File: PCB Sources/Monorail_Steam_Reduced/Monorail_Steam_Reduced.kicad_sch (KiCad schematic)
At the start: 185 parts, among them J1 USB_C_Receptacle_USB2.0, J10 Conn_01x09, J2 USB_C_Receptacle_USB2.0, J4 Conn_01x04_Male, J5 Conn_01x04_Female, J6 Conn_01x03_Male, J7 Conn_01x09, J8 Conn_01x05, J9 Conn_01x05, SW1 RotaryEncoder_Switch, SW2 RotaryEncoder_Switch, SW3 RotaryEncoder_Switch, U1 SRV05-4, U2 XC6206PxxxMR, U3 RP2040TR7, U4 W25Q128JVS, Y1 Crystal_GND24_Small

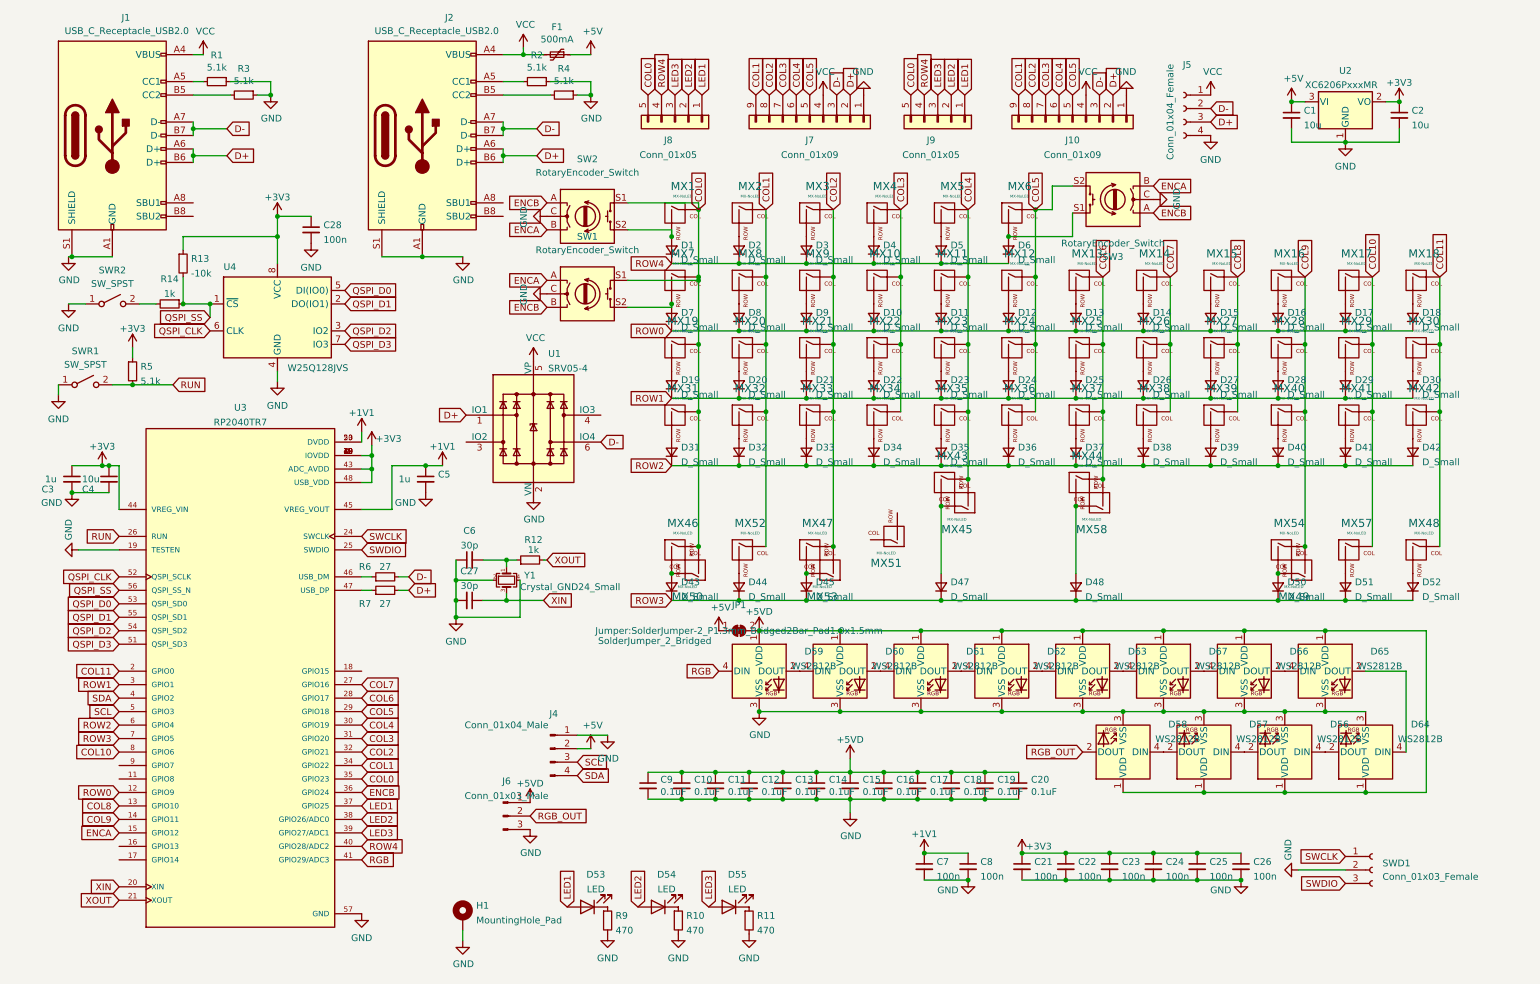
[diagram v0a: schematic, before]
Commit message: updated pcb: deleted num-row, new bottom row
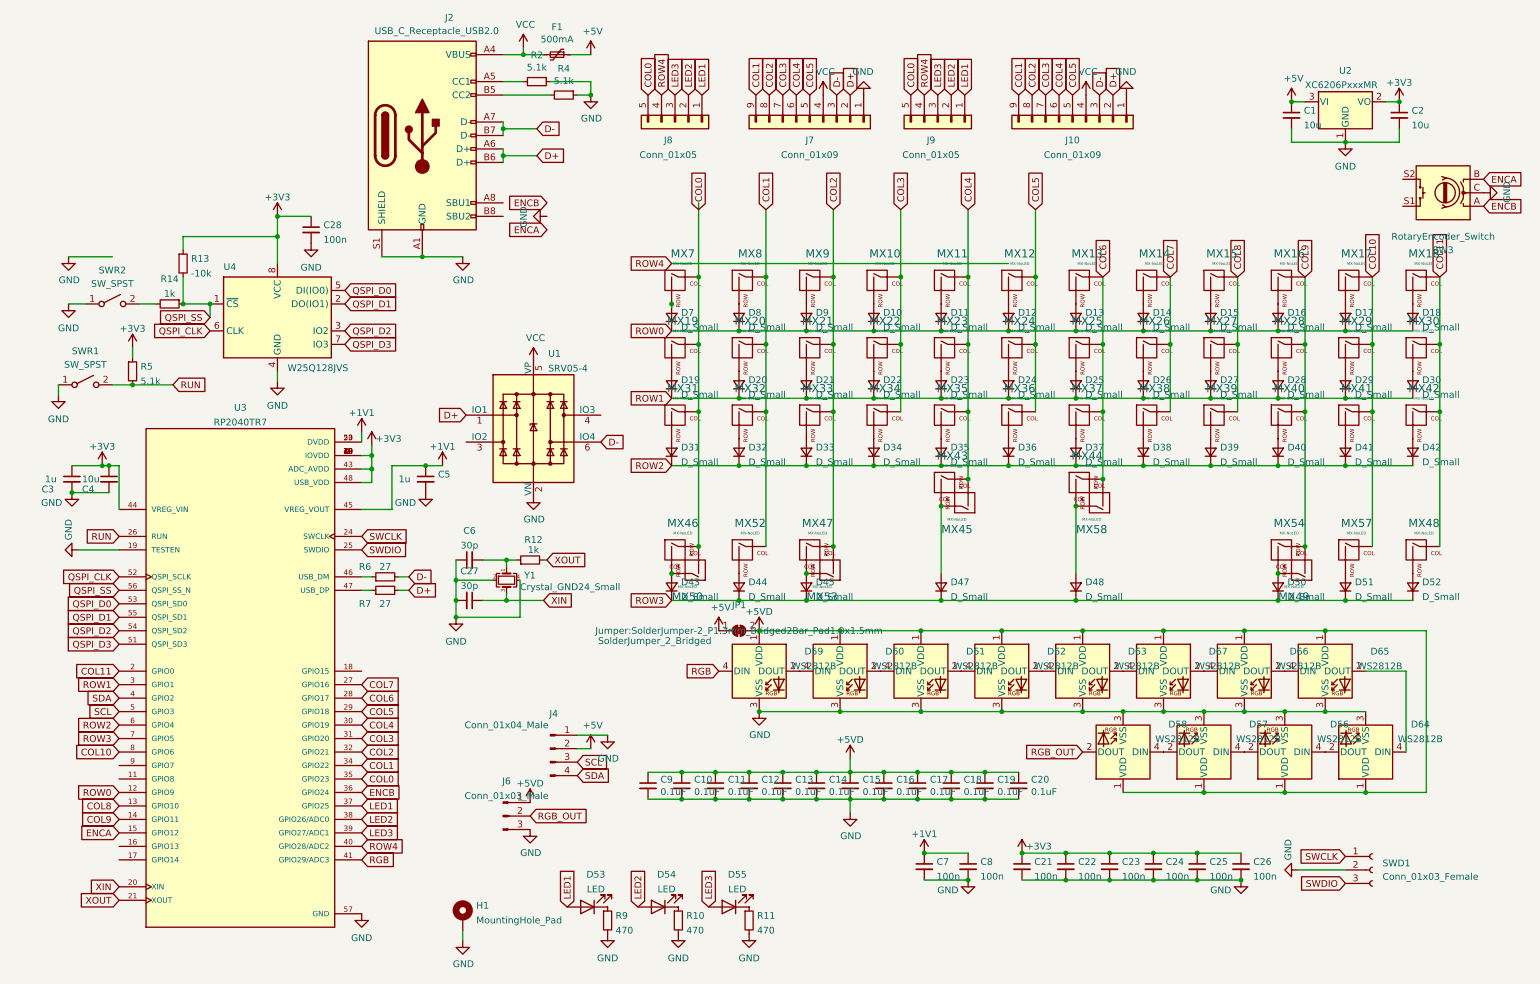
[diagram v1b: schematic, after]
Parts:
- removed D1, D2, D3, D4, D5, D6: D_Small, Diode_SMD:D_SOD-123, symbol Device:D_Small
- removed J1: USB_C_Receptacle_USB2.0, Keebio-Parts:USB_C_Receptacle_HRO_TYPE-C-31-M-12, symbol Connector:USB_C_Receptacle_USB2.0
- removed J5: Conn_01x04_Female, Connector_JST:JST_SH_SM04B-SRSS-TB_1x04-1MP_P1.00mm_Horizontal, symbol Connector:Conn_01x04_Female
- removed MX1, MX2, MX3, MX4, MX5, MX6: MX-NoLED, MX_Only:MXOnly-1U-Hotswap, symbol MX_Alps_Hybrid:MX-NoLED
- removed MX51: MX-NoLED, MX_Only:MXOnly-1.25U-Hotswap, symbol MX_Alps_Hybrid:MX-NoLED
- removed R1, R3: 5.1k, Resistor_SMD:R_0603_1608Metric, symbol Device:R_Small
- removed SW1, SW2: RotaryEncoder_Switch, kiserdesigns:RotaryEncoder_Alps_EC11E-Switch_Vertical_H20mm, symbol Device:RotaryEncoder_Switch
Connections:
- net COL5: no longer SW3.S2
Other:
- moved on the sheet: SW3

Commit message: removed unecessary files, cleaned pcb
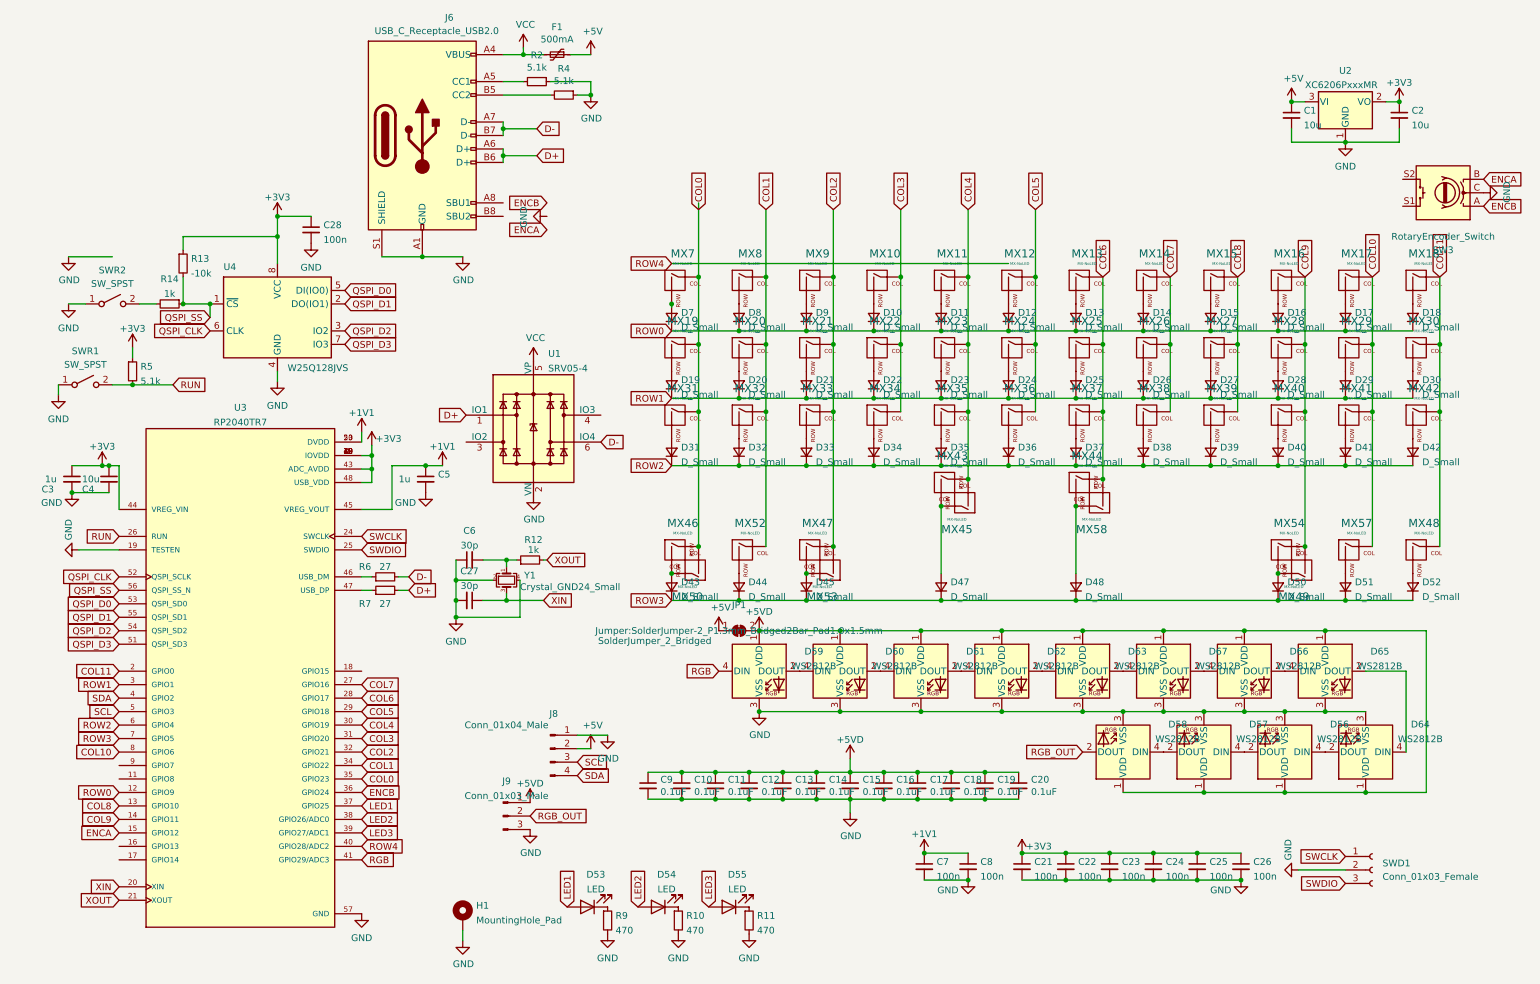
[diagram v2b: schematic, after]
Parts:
- removed J10, J7: Conn_01x09, Connector_PinHeader_2.54mm:PinHeader_1x09_P2.54mm_Vertical, symbol Connector_Generic:Conn_01x09
- removed J8, J9: Conn_01x05, Connector_PinHeader_2.54mm:PinHeader_1x05_P2.54mm_Vertical, symbol Connector_Generic:Conn_01x05
- renumbered J2 to J6, J4 to J8, J6 to J9

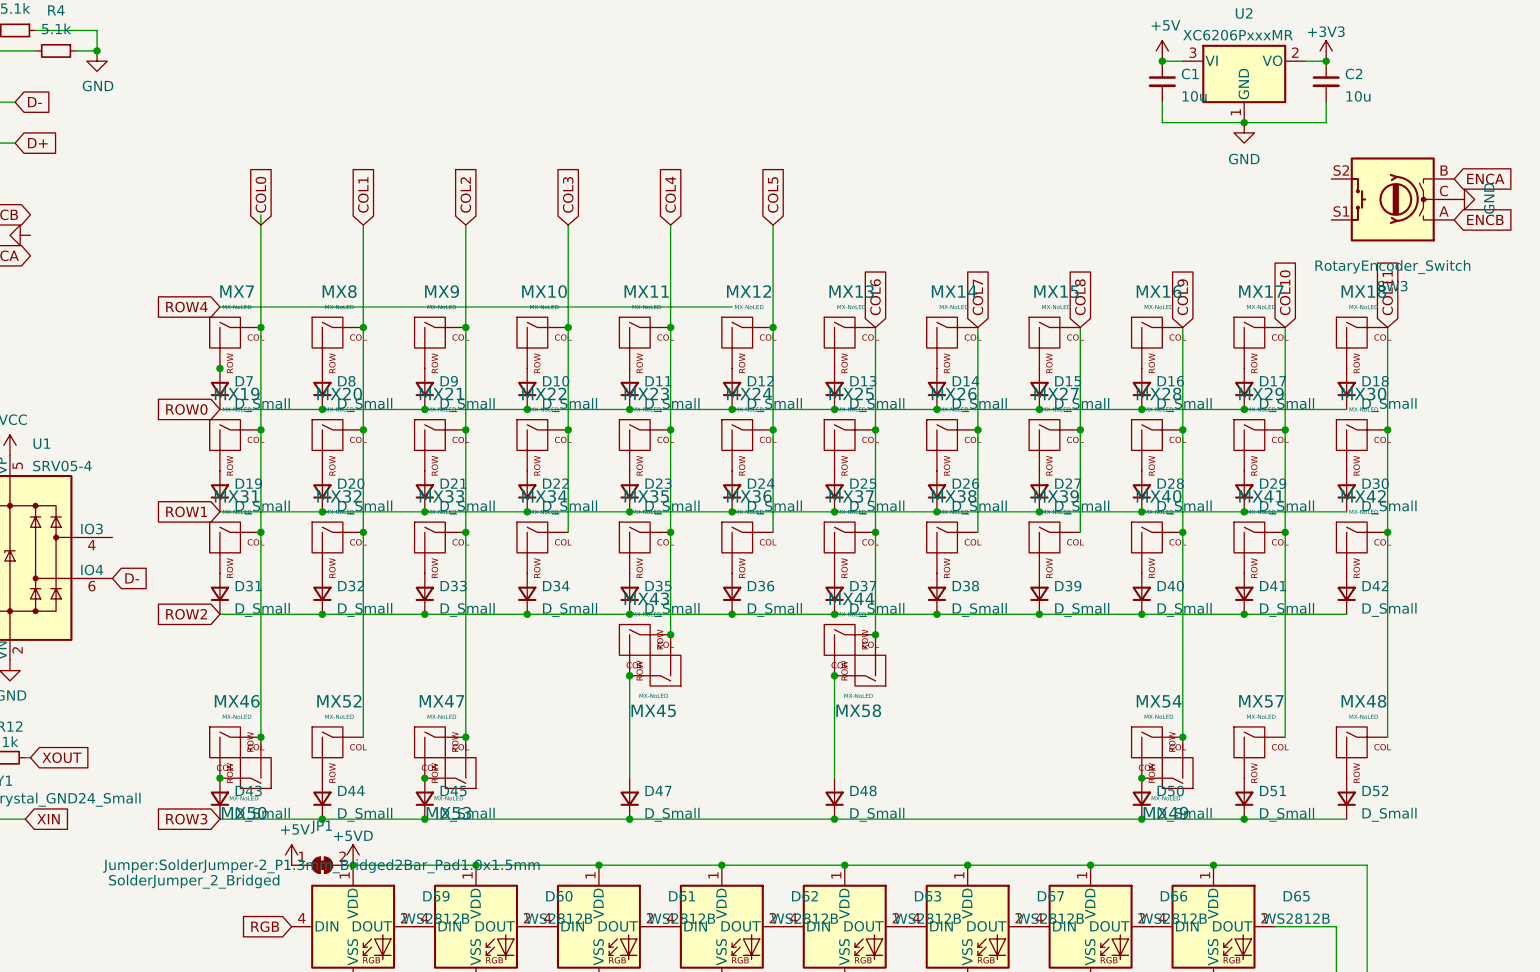
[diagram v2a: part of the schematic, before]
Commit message: updated positions, readme, deleted unecessary files
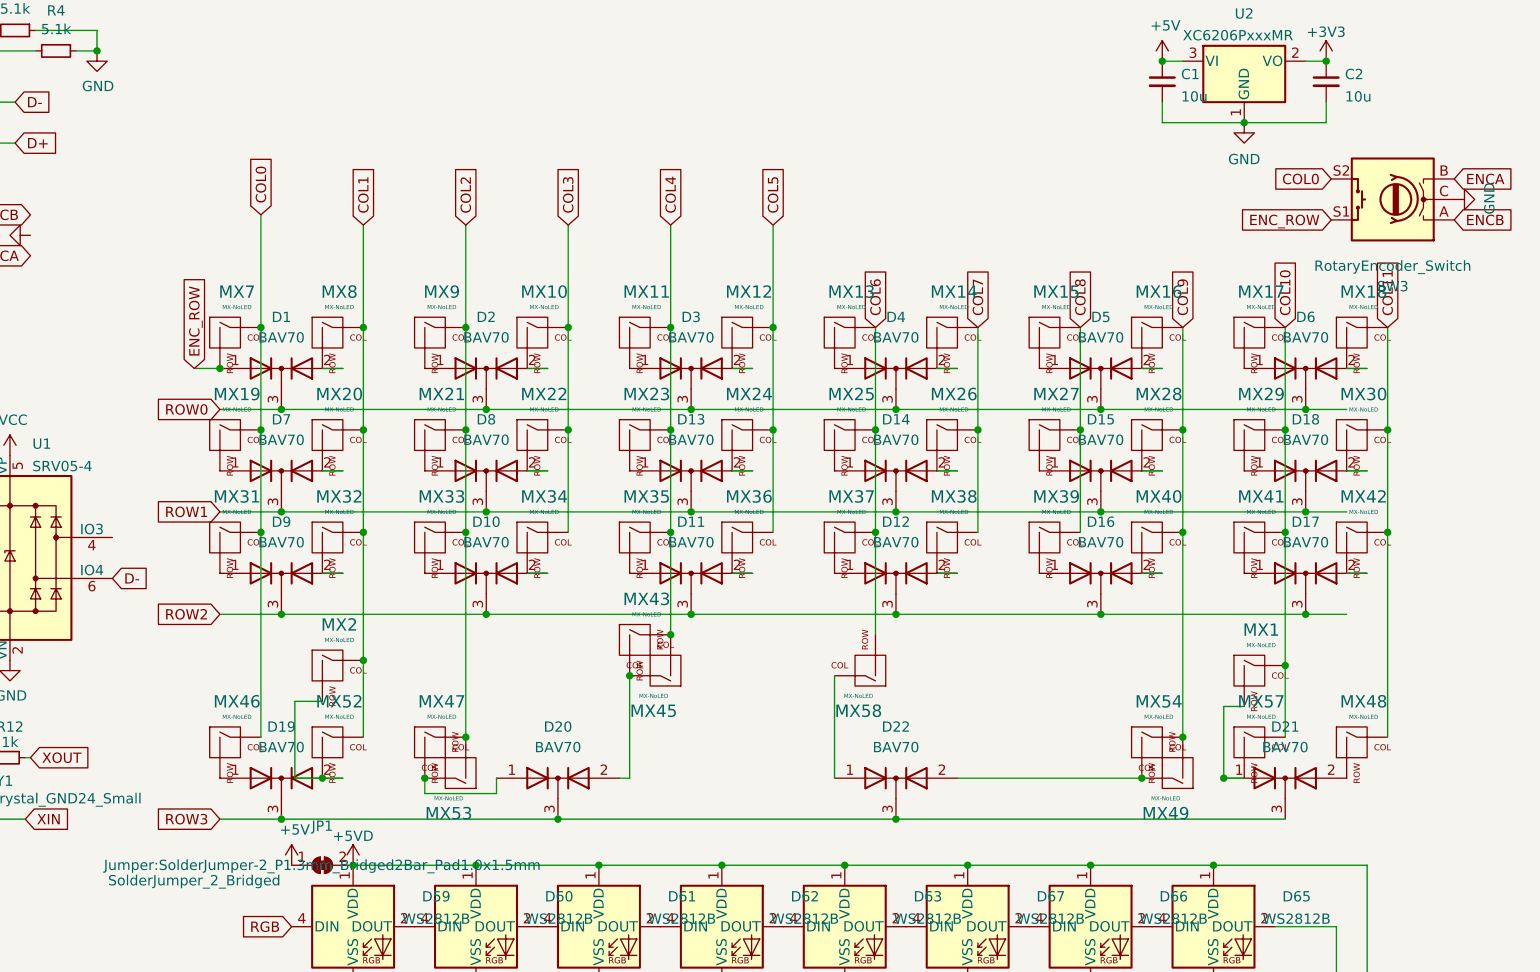
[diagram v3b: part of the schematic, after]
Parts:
- removed D10, D11, D12, D13, D14, D15, D16, D17, D18, D19, D20, D21, D22, D23, D24, D25, D26, D27, D28, D29, D30, D31, D32, D33, D34, D35, D36, D37, D38, D39, D40, D41, D42, D43, D44, D45, D47, D48, D50, D51, D52, D7, D8, D9: D_Small, Diode_SMD:D_SOD-123, symbol Device:D_Small
- removed MX44: MX-NoLED, MX_Only:MXOnly-3U-Hotswap-ReversedStabilizers, symbol MX_Alps_Hybrid:MX-NoLED
- removed MX50: MX-NoLED, MX_Only:MXOnly-1.25U-Hotswap, symbol MX_Alps_Hybrid:MX-NoLED
- added D1, D10, D11, D12, D13, D14, D15, D16, D17, D18, D19, D2, D20, D21, D22, D3, D4, D5, D6, D7, D8, D9: BAV70, Package_TO_SOT_SMD:SOT-23, symbol Diode:BAV70
- added MX1, MX2: MX-NoLED, marbastlib-mx:SW_MX_HS_1u_NOREF, symbol MX_Alps_Hybrid:MX-NoLED
- D56, D57, D58, D59, D60, D61, D62, D63, D64, D65, D66, D67: footprint Keebio-Parts:LED_WS2812B_2020 -> WS2812B:WS2812B_data-bridgeable
- J6: footprint Keebio-Parts:USB_C_Receptacle_HRO_TYPE-C-31-M-12 -> Type-C:HRO-TYPE-C-31-M-12-Assembly
- MX10, MX11, MX12, MX13, MX14, MX15, MX16, MX17, MX20, MX21, MX22, MX23, MX24, MX25, MX26, MX27, MX28, MX29, MX32, MX33, MX34, MX35, MX36, MX37, MX38, MX39, MX40, MX41, MX42, MX46, MX47, MX49, MX52, MX57, MX7, MX8, MX9: footprint MX_Only:MXOnly-1U-Hotswap -> marbastlib-mx:SW_MX_HS_1u_NOREF
- MX18, MX31: footprint MX_Only:MXOnly-1.75U-Hotswap -> marbastlib-mx:SW_MX_HS_1u_NOREF
- MX19, MX48, MX53, MX54: footprint MX_Only:MXOnly-1.25U-Hotswap -> marbastlib-mx:SW_MX_HS_1u_NOREF
- MX30: footprint MX_Only:MXOnly-1.5U-Hotswap -> marbastlib-mx:SW_MX_HS_1u_NOREF
- MX43: footprint MX_Only:MXOnly-3U-Hotswap-ReversedStabilizers -> marbastlib-mx:SW_MX_HS_1u_NOREF
- MX45: footprint MX_Only:MXOnly-2.75U-Hotswap -> marbastlib-mx:SW_MX_HS_1u_NOREF
- MX58: footprint MX_Only:MXOnly-6.25U-Hotswap-ReversedStabilizers -> marbastlib-mx:SW_MX_HS_1u_NOREF
- SW3: footprint kiserdesigns:RotaryEncoder_Alps_EC11E-Switch_Vertical_H20mm -> marbastlib-various:ROT_Alps_EC11E-Switch
- U3: footprint SnapEDA Library:QFN40P700X700X90-57N -> cipulot_kicad_parts:RP2040-QFN-56
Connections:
- net COL0: now also SW3.S2
- net COL1: now also MX2.1 (COL)
- net COL10: now also MX1.1 (COL)
- net ROW0: now also D1.3 (K), D2.3 (K), D3.3 (K), D4.3 (K), D5.3 (K), D6.3 (K)
- net ROW1: now also D13.3 (K), D14.3 (K), D15.3 (K), D18.3 (K), D7.3 (K), D8.3 (K)
- net ROW2: now also D10.3 (K), D11.3 (K), D12.3 (K), D16.3 (K), D17.3 (K), D9.3 (K)
- net ROW3: now also D19.3 (K), D20.3 (K), D21.3 (K), D22.3 (K)
- net at MX49.1 (COL), MX54.2 (ROW): now also D22.2 (A)
- net ENC_ROW: now reaches MX7.2 (ROW)
- net ENC_ROW: now also SW3.S1, D1.1 (A)
- net at MX8.2 (ROW): now also D1.2 (A)
- net at MX9.2 (ROW): now also D2.1 (A)
- net at MX10.2 (ROW): now also D2.2 (A)
- net at MX11.2 (ROW): now also D3.1 (A)
- net at MX12.2 (ROW): now also D3.2 (A)
- net at MX13.2 (ROW): now also D4.1 (A)
- net at MX14.2 (ROW): now also D4.2 (A)
- net at MX15.2 (ROW): now also D5.1 (A)
- net at MX16.2 (ROW): now also D5.2 (A)
- net at MX17.2 (ROW): now also D6.1 (A)
- net at MX18.2 (ROW): now also D6.2 (A)
- net at MX19.2 (ROW): now also D7.1 (A)
- net at MX20.2 (ROW): now also D7.2 (A)
- net at MX21.2 (ROW): now also D8.1 (A)
- net at MX22.2 (ROW): now also D8.2 (A)
- net at MX23.2 (ROW): now also D13.1 (A)
- net at MX24.2 (ROW): now also D13.2 (A)
- net at MX25.2 (ROW): now also D14.1 (A)
- net at MX26.2 (ROW): now also D14.2 (A)
- net at MX27.2 (ROW): now also D15.1 (A)
- net at MX28.2 (ROW): now also D15.2 (A)
- net at MX29.2 (ROW): now also D18.1 (A)
- net at MX30.2 (ROW): now also D18.2 (A)
- net at MX31.2 (ROW): now also D9.1 (A)
- net at MX32.2 (ROW): now also D9.2 (A)
- net at MX33.2 (ROW): now also D10.1 (A)
- net at MX34.2 (ROW): now also D10.2 (A)
- net at MX35.2 (ROW): now also D11.1 (A)
- net at MX36.2 (ROW): now also D11.2 (A)
- net at MX37.2 (ROW): now also D12.1 (A)
- net at MX38.2 (ROW): now also D12.2 (A)
- net at MX39.2 (ROW): now also D16.1 (A)
- net at MX40.2 (ROW): now also D16.2 (A)
- net at MX41.2 (ROW): now also D17.1 (A)
- net at MX42.2 (ROW): now also D17.2 (A)
- net at MX46.2 (ROW): now also D19.1 (A)
- net at MX48.2 (ROW): now also D21.2 (A)
- net at MX52.2 (ROW): now also D19.2 (A), MX2.2 (ROW)
- net at MX43.2 (ROW), MX45.1 (COL): now also D20.2 (A)
- net at MX57.2 (ROW): now also D21.1 (A), MX1.2 (ROW)
- net at MX47.2 (ROW), MX53.1 (COL): now also D20.1 (A)
- net at MX58.1 (COL): now also D22.1 (A)
